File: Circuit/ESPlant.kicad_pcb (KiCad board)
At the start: 2 copper layers, 97 x 77.5 mm, 68 parts, among them P1 SOIL, P101 CONN_DIGITAL, P102 CONN_ANALOG, P103 CONN_SERIAL, P104 CONN_I2C, P105 SOLAR, P106 USB_5PIN_SHELL, P109 CONN_PWR, P110 CONN_01X05, P111 UV, P112 TEMP, P113 NEOPIXEL, P114 PIR, Q101 FDN340P, Q201 FDN340P, Q202 FDN340P, Q203 FDN340P, SW101 RESET, SW102 PRGM, SW103 RESET, U101 STM32F042F, U103 ESP-12E, U201 CN3063, U202 MCP6002, U301 BME280, U302 ADXL345

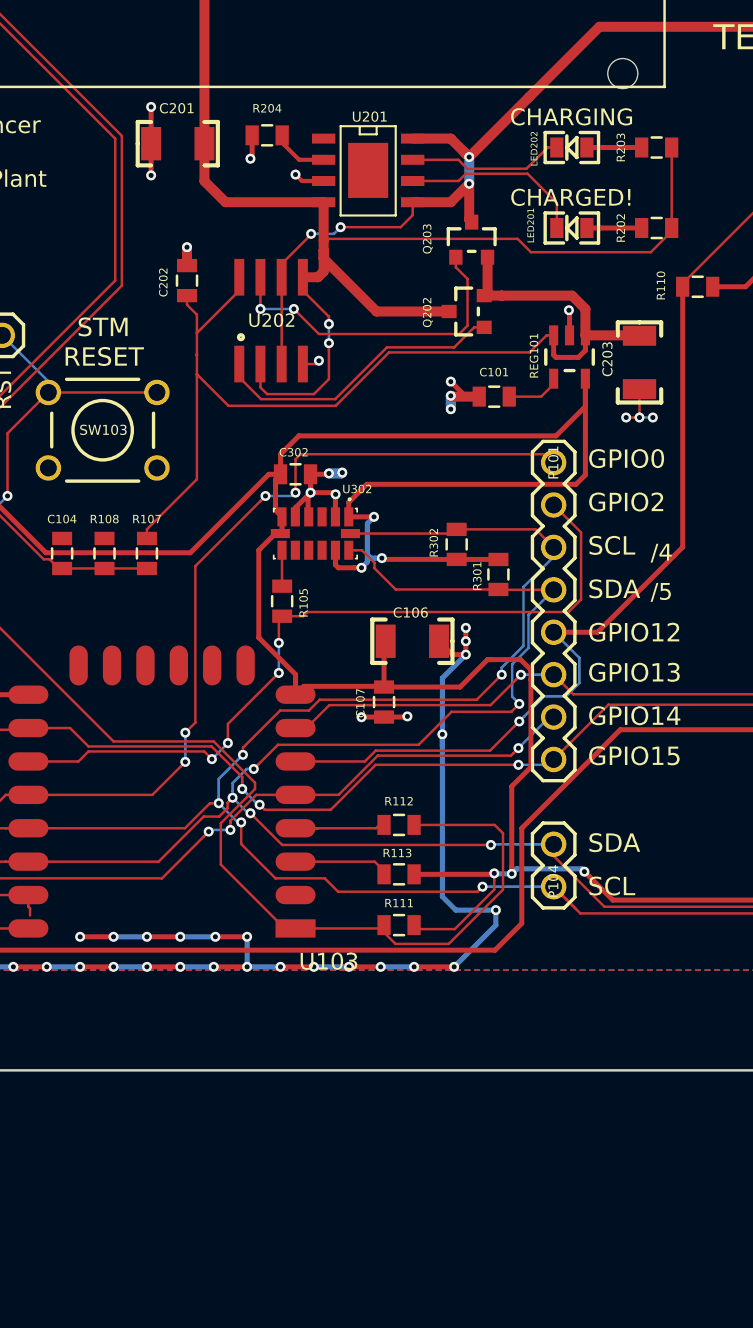
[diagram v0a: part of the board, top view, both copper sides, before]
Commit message: Downsize 0805s to 0603 for @jonoxer's pnp machine :)
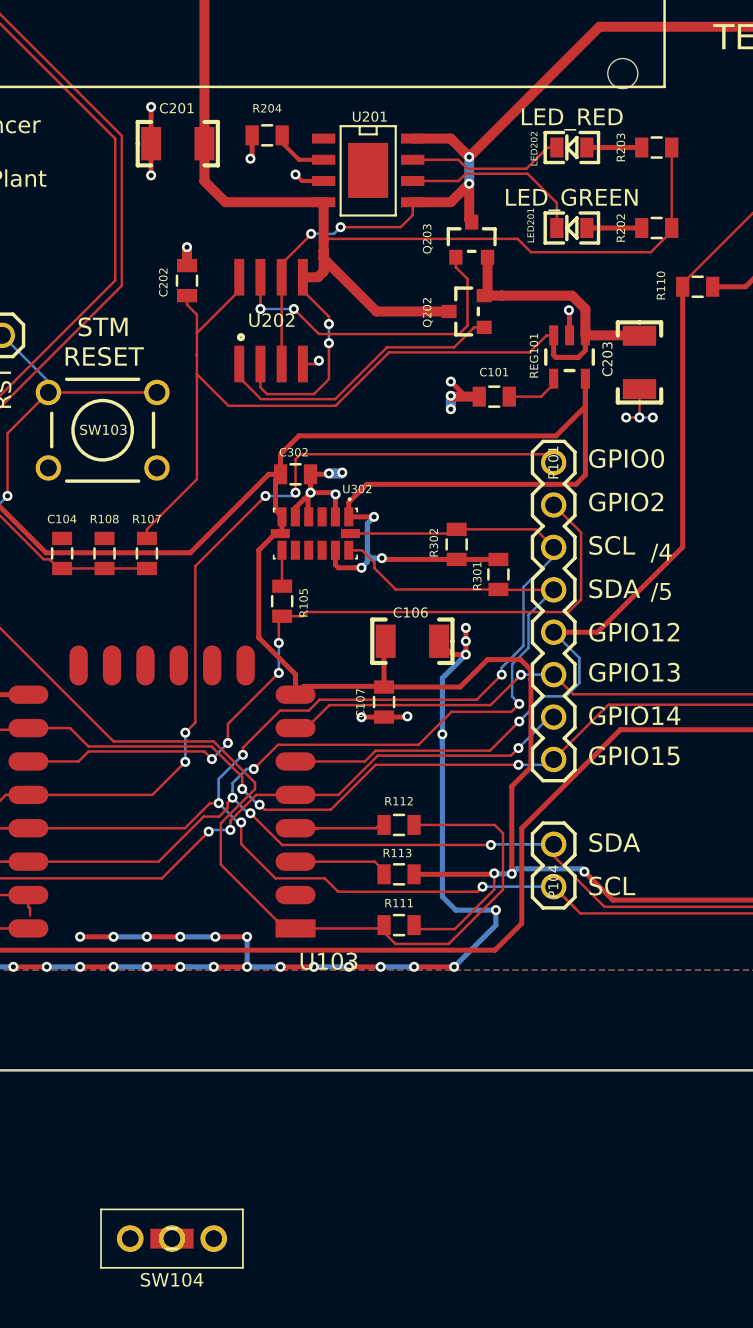
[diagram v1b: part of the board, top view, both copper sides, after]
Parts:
- added R114: 10K, FT:0805, F.Cu at (190.5, 148.1)
- added SW104: SS12D00, Plant:SS12D00, F.Cu at (190.5, 148.1)
- C106, C203: value 220uF 16V -> 100uF 16V X5R
- LED201: value CHARGED! -> LED_GREEN
- LED202: value CHARGING -> LED_RED
- R101: value 10K DNP -> 1K
- R112: value 10K -> 1K
- R202, R203: value 330R -> 1K
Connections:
- P102 pad 4: (no net) -> /SOIL_1
- P102 pad 5: /SOIL_1 -> /SOIL_2
- P102 pad 6: /SOIL_2 -> GND
- Q101 pad D: +3V3 -> /VCC_SENS
- Q101 pad S: /VCC_SENS -> +3V3
- R101 pad 1: /GPIO0 -> /GPIO0_BOOT
- R101 pad 2: GND -> /GPIO0
- REG101 pad 1: /Power/VOUT -> /VSWITCHED
- REG101 pad 3: /Power/VOUT -> /VSWITCHED
- SW102 pad 2: /GPIO0 -> /GPIO0_BOOT
- U101 pad 1: /GPIO0 -> /GPIO0_BOOT
- U103 pad 19: /I2C Sensors/I2C_SCL -> /I2C Sensors/I2C_SDA
- U103 pad 20: /I2C Sensors/I2C_SDA -> /I2C Sensors/I2C_SCL
- U301 pad 5: GND -> +3V3
- U302 pad 12: +3V3 -> GND
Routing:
- net /GPIO0_BOOT: track 0.00 -> 74.6 mm, vias 0 -> 3
- net /GPIO0: track 136.4 -> 67.5 mm
- net /I2C Sensors/I2C_SCL: track 128.5 -> 110.4 mm, vias 5 -> 3
- net /I2C Sensors/I2C_SDA: track 125.8 -> 143.9 mm, vias 5 -> 7
- net /SOIL_2: track 41.3 -> 24.9 mm
- net /VSWITCHED: track 0.00 -> 9.43 mm
- net /Power/VOUT: track 62.4 -> 53.0 mm
- net GND: track 153.3 -> 161.0 mm, vias 62 -> 58
- net +3V3: track 225.6 -> 229.3 mm, vias 10 -> 11
- net /SOIL_1: track 32.7 -> 32.0 mm

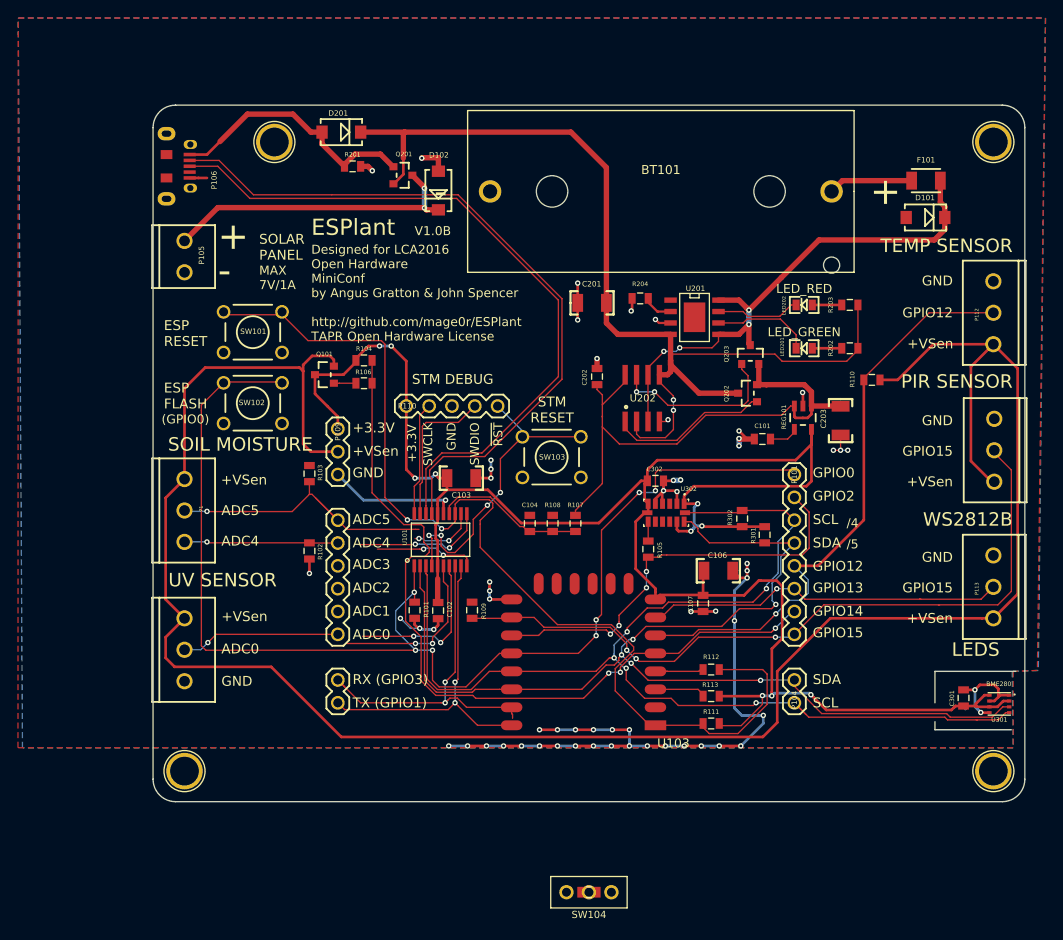
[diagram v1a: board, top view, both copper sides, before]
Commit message: V1.1 reroutes, excluding 0805->0603
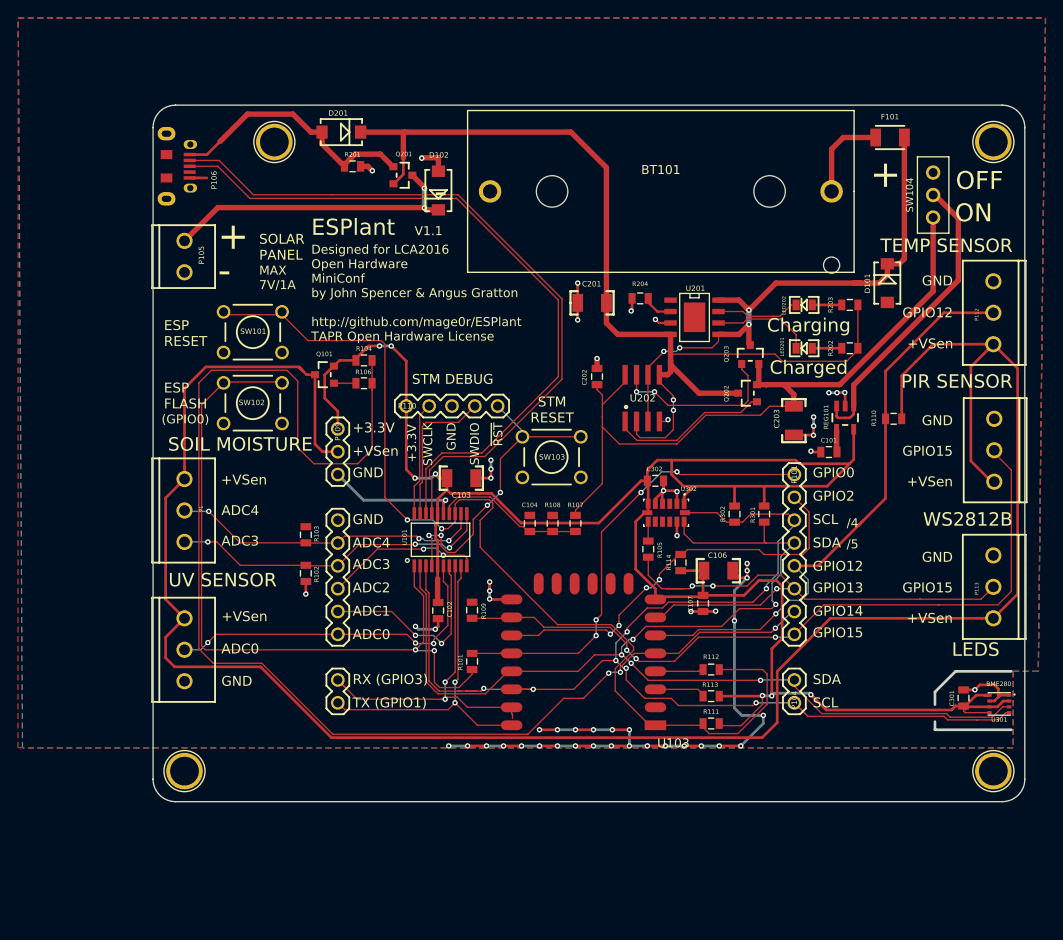
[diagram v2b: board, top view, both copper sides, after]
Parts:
- C101: value 100nF -> 100nF 6.3V
- R102, R103: value 100K -> 100K 1%
- R107: value 56K 1% -> 121K 1%
- R108: value 47K 1% -> 100K 1%
- moved SW104 86.5 mm to (228.8, 70.5), turned to 90 degrees
- moved R114 38.1 mm to (200.7, 111.4), turned to 90 degrees
- moved R101 8.57 mm to (177.5, 122.4), turned to 90 degrees
- moved D101 8.45 mm to (223.7, 80.3), turned to 90 degrees
- moved C101 7.54 mm to (217.2, 99.1)
- moved R103 6.81 mm to (159.0, 108.3)
- moved F101 6.25 mm to (224.0, 64.1)
- moved C203 5.20 mm to (213.3, 95.6)
- moved R110 4.96 mm to (224.4, 95.4)
- moved REG101 4.70 mm to (219.0, 95.3)
- moved R102 2.53 mm to (159.0, 112.6)
- moved R301 2.30 mm to (210.0, 106.0)
- moved R302 0.99 mm to (206.7, 106.0), turned to 270 degrees
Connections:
- R105 pad 1: /GPIO2 -> /GPIO13
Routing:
- net /GPIO14: track 88.8 -> 144.8 mm
- net /Power/VOUT: track 53.0 -> 82.1 mm
- net /I2C Sensors/I2C_SCL: track 110.4 -> 135.8 mm, vias 3 -> 7
- net /VSWITCHED: track 9.43 -> 33.9 mm
- net /GPIO13: track 40.1 -> 63.0 mm, vias 1 -> 3
- net GND: track 161.0 -> 144.7 mm, vias 58 -> 59
- net /GPIO0: track 67.5 -> 52.1 mm, vias 7 -> 4
- net /I2C Sensors/I2C_SDA: track 143.9 -> 128.7 mm, vias 7 -> 5
- net /SOIL_2: track 24.9 -> 35.7 mm
- net /GPIO0_BOOT: track 74.6 -> 81.8 mm, vias 3 -> 2
- net /ADC2: track 11.3 -> 17.6 mm
- net /SOIL_1: track 32.0 -> 36.3 mm
- net /ADC1: track 18.1 -> 22.2 mm
- net /Power/VBAT: track 62.2 -> 66.1 mm
- net /VCC_SENS: track 233.9 -> 231.3 mm
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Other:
- outline, holes or cut-outs redrawn
- board text added: "Charged"
- board text added: "Charging"
- board text added: "Designed for LCA2016 Open Hardware MiniConf by John Spencer & Angus Gratton http://github.com/mage0r/ESPlant TAPR Open Hardware License"
- board text added: "OFF"
- board text added: "ON"
- board text added: "V1.1"
- board text removed: "ADC5"
- board text removed: "Designed for LCA2016 Open Hardware MiniConf by Angus Gratton & John Spencer http://github.com/mage0r/ESPlant TAPR Open Hardware License"
- board text removed: "V1.0B"

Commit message: Shrink to 0603, some other cleanups
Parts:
- C101, C102, C107, C202, C301, C302: footprint FT:0805 -> FT:0603_CAP
- C104, R101, R102, R103, R104, R105, R106, R107, R108, R109, R110, R111, R112, R113, R114, R201, R202, R203, R204, R301, R302: footprint FT:0805 -> FT:0603
- moved SW104 3.01 mm to (225.8, 70.3)
- moved F101 2.51 mm to (226.5, 63.9)
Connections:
- P101 pad 3: /I2C Sensors/I2C_SCL -> /I2C Sensors/I2C_SDA
- P101 pad 4: /I2C Sensors/I2C_SDA -> /I2C Sensors/I2C_SCL
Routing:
- net GND: track 144.7 -> 152.6 mm, vias 59 -> 63
- net /I2C Sensors/I2C_SDA: track 128.7 -> 136.5 mm, vias 5 -> 6
- net Net-(C104-Pad1): track 16.9 -> 23.6 mm
- net /Power/VBAT: track 66.1 -> 69.7 mm
- net /GPIO13: track 63.0 -> 61.0 mm
- net /VSWITCHED: track 33.9 -> 31.9 mm
- net /BAT+: track 10.1 -> 12.1 mm
- net /Power/VOUT: track 82.1 -> 80.9 mm
- net +3V3: track 230.7 -> 229.5 mm, vias 7 -> 9
- net /I2C Sensors/I2C_SCL: track 135.8 -> 135.3 mm
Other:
- board text added: "SCL/GPIO5"
- board text added: "SDA/GPIO4"
- board text removed: "/4"
- board text removed: "/5"

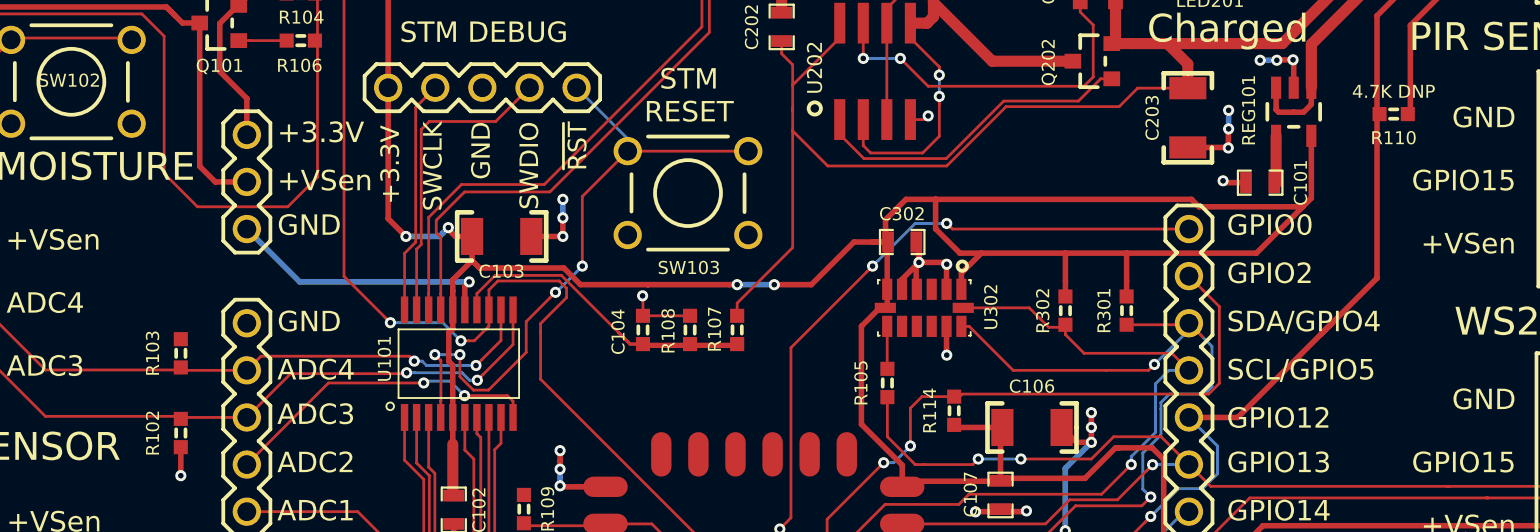
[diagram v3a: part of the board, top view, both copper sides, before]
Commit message: Add cable tie holes, V1.1 production candidate?
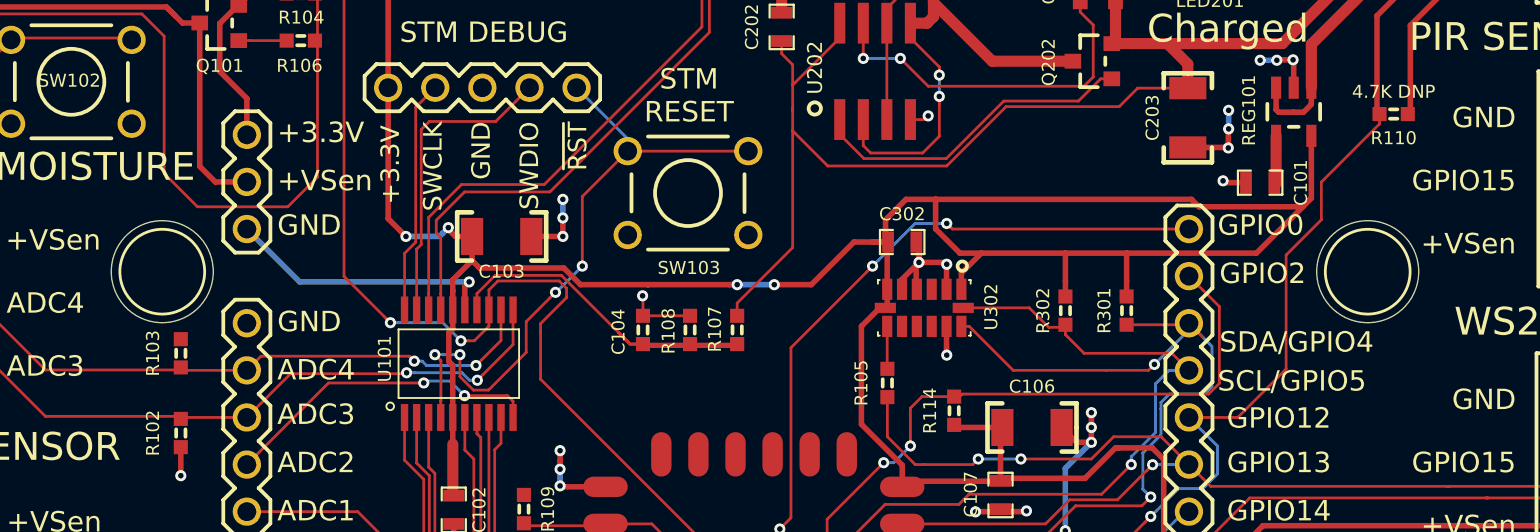
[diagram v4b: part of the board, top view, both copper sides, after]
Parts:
- added 1pin: VAL**, Connect:1pin, F.Cu at (223.0, 103.9)
- added 1pin: VAL**, Connect:1pin, F.Cu at (158.0, 103.9)
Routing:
- net /GPIO12: track 65.5 -> 64.8 mm
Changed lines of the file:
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@@
 (kicad_pcb (version 4) (host pcbnew 0.201511110417+6307~30~ubuntu15.10.1-product)
   (general
-    (links 184)
+    (links 0)
     (no_connects 0)
-    (area 141.924999 60.424999 239.075001 138.075001)
+    (area 126.97 50.8 241.300001 138.419)
     (thickness 1.6)
     (drawings 128)
-    (tracks 1085)
+    (tracks 1087)
     (zones 0)
-    (modules 70)
+    (modules 72)
     (nets 46)
   )
@@
   )
   (setup
-    (last_trace_width 0.6)
+    (last_trace_width 0.15)
     (user_trace_width 0.15)
     (user_trace_width 0.2)
@@
     (add_net /USB_D-)
   )
+  (module Connect:1pin (layer F.Cu)
+    (at 223 103.9)
+    (descr "module 1 pin (ou trou mecanique de percage)")
+    (tags DEV)
+    (fp_text reference 1pin (at 0 -3.048) (layer F.SilkS) hide
+      (effects (font (size 1 1) (thickness 0.15)))
+    )
+    (fp_text value VAL** (at 0 2.794) (layer F.SilkS) hide
+      (effects (font (size 1 1) (thickness 0.15)))
+    )
+    (fp_circle (center 0 0) (end 0 -2.286) (layer F.SilkS) (width 0.15))
+    (pad "" np_thru_hole circle (at 0 0) (size 5.5 5.5) (drill 5.5) (layers *.Cu *.Mask F.SilkS))
+  )
+  (module Connect:1pin (layer F.Cu)
+    (at 158 103.9)
+    (descr "module 1 pin (ou trou mecanique de percage)")
+    (tags DEV)
+    (fp_text reference 1pin (at 0 -3.048) (layer F.SilkS) hide
+      (effects (font (size 1 1) (thickness 0.15)))
+    )
+    (fp_text value VAL** (at 0 2.794) (layer F.SilkS) hide
+      (effects (font (size 1 1) (thickness 0.15)))
+    )
+    (fp_circle (center 0 0) (end 0 -2.286) (layer F.SilkS) (width 0.15))
+    (pad "" np_thru_hole circle (at 0 0) (size 5.5 5.5) (drill 5.5) (layers *.Cu *.Mask F.SilkS))
+  )
   (module Plant:ADXL345 (layer F.Cu)
     (at 199.09 105.85 270)
@@
     )
   )
-  (gr_text SCL/GPIO5 (at 224.5 109.2) (layer B.SilkS)
+  (gr_text SCL/GPIO5 (at 224 109.8) (layer B.SilkS)
     (effects (font (size 1.1 1.1) (thickness 0.2)) (justify left mirror))
   )
-  (gr_text SDA/GPIO4 (at 224.4 106.6) (layer B.SilkS)
+  (gr_text SDA/GPIO4 (at 224.1 107.8) (layer B.SilkS)
     (effects (font (size 1.1 1.1) (thickness 0.2)) (justify left mirror))
   )
@@
     (effects (font (size 1.1 1.1) (thickness 0.2)) (justify left mirror))
   )
-  (gr_text "GPIO0\n" (at 220.4139 101.395) (layer B.SilkS)
+  (gr_text "GPIO0\n" (at 219.9 101.395) (layer B.SilkS)
     (effects (font (size 1.1 1.1) (thickness 0.2)) (justify left mirror))
   )
-  (gr_text GPIO2 (at 220.4266 103.9858) (layer B.SilkS)
+  (gr_text GPIO2 (at 219.9 103.9858) (layer B.SilkS)
     (effects (font (size 1.1 1.1) (thickness 0.2)) (justify left mirror))
   )
@@
     (effects (font (size 1.1 1.1) (thickness 0.2)) (justify left))
   )
-  (gr_text SCL/GPIO5 (at 215.4 109.2) (layer F.SilkS)
+  (gr_text SCL/GPIO5 (at 214.9 109.8) (layer F.SilkS)
     (effects (font (size 1.1 1.1) (thickness 0.2)) (justify left))
   )
-  (gr_text SDA/GPIO4 (at 215.4 106.6) (layer F.SilkS)
+  (gr_text SDA/GPIO4 (at 215 107.7) (layer F.SilkS)
     (effects (font (size 1.1 1.1) (thickness 0.2)) (justify left))
   )
-  (gr_text GPIO2 (at 215.4 104) (layer F.SilkS)
+  (gr_text GPIO2 (at 215 104) (layer F.SilkS)
     (effects (font (size 1.1 1.1) (thickness 0.2)) (justify left))
   )
-  (gr_text "GPIO0\n" (at 215.4 101.4) (layer F.SilkS)
+  (gr_text "GPIO0\n" (at 214.9 101.4) (layer F.SilkS)
     (effects (font (size 1.1 1.1) (thickness 0.2)) (justify left))
   )
@@
   (segment (start 213.36 124.46) (end 209.640008 124.46) (width 0.15) (layer B.Cu) (net 20))
   (segment (start 201.1 106.86) (end 201.09 106.85) (width 0.15) (layer F.Cu) (net 20))
+  (segment (start 215.99 111.76) (end 213.36 111.76) (width 0.15) (layer F.Cu) (net 21))
+  (segment (start 223.638 95.4) (end 223.638 95.931) (width 0.15) (layer F.Cu) (net 21))
+  (segment (start 223.638 95.931) (end 220.5 99.069) (width 0.15) (layer F.Cu) (net 21))
+  (segment (start 220.5 99.069) (end 220.5 101.1) (width 0.15) (layer F.Cu) (net 21))
+  (segment (start 220.5 101.1) (end 218.6 103) (width 0.15) (layer F.Cu) (net 21))
+  (segment (start 218.6 103) (end 218.6 109.15) (width 0.15) (layer F.Cu) (net 21))
+  (segment (start 218.6 109.15) (end 215.99 111.76) (width 0.15) (layer F.Cu) (net 21))
   (segment (start 197.9 119.5) (end 201.8 119.5) (width 0.15) (layer F.Cu) (net 21))
   (segment (start 201.8 119.5) (end 202.35 118.95) (width 0.15) (layer F.Cu) (net 21))
@@
   (segment (start 223.50084 90.09916) (end 229.99758 83.60242) (width 0.3) (layer F.Cu) (net 21))
   (segment (start 229.99758 83.60242) (end 235.5 83.60242) (width 0.3) (layer F.Cu) (net 21))
-  (segment (start 220.5 107.25) (end 215.99 111.76) (width 0.3) (layer F.Cu) (net 21))
-  (segment (start 221.08668 106.66332) (end 220.5 107.25) (width 0.3) (layer F.Cu) (net 21))
-  (segment (start 220.5 107.25) (end 223.50084 104.24916) (width 0.3) (layer F.Cu) (net 21))
-  (segment (start 223.50084 104.24916) (end 223.50084 95.4) (width 0.3) (layer F.Cu) (net 21))
   (segment (start 211.599999 116.800001) (end 211.3 117.1) (width 0.15) (layer B.Cu) (net 21))
   (segment (start 212.8 115.6) (end 211.599999 116.800001) (width 0.15) (layer B.Cu) (net 21))
@@
   (via (at 211.3 117.1) (size 0.6) (drill 0.3) (layers F.Cu B.Cu) (net 21))
   (segment (start 213.36 111.76) (end 214.9 113.3) (width 0.15) (layer B.Cu) (net 21))
-  (segment (start 215.99 111.76) (end 213.36 111.76) (width 0.3) (layer F.Cu) (net 21))
   (segment (start 197.9 117.5) (end 205.625002 117.5) (width 0.15) (layer F.Cu) (net 22))
   (segment (start 205.625002 117.5) (end 206.924991 116.200011) (width 0.15) (layer F.Cu) (net 22))
